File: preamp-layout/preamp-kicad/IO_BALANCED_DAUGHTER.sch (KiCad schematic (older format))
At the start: 49 parts, among them J29 XLR3, J30 XLR3, J31 Conn_01x03_Male, J32 Conn_01x03_Female, J33 Conn_01x03_Female, J34 Conn_01x03_Male, J35 XLR3, J36 XLR3, U6 TL072, U7 TL072, U8 TL072

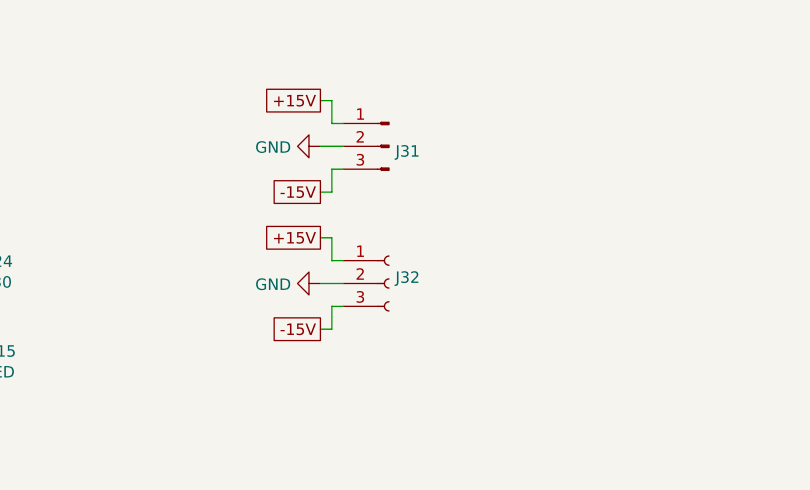
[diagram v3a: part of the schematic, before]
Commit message: power headers updated, slight BOM update
changed footprint on all 5V, +-15V to JST B2B / B3B connectors. All male conns now.
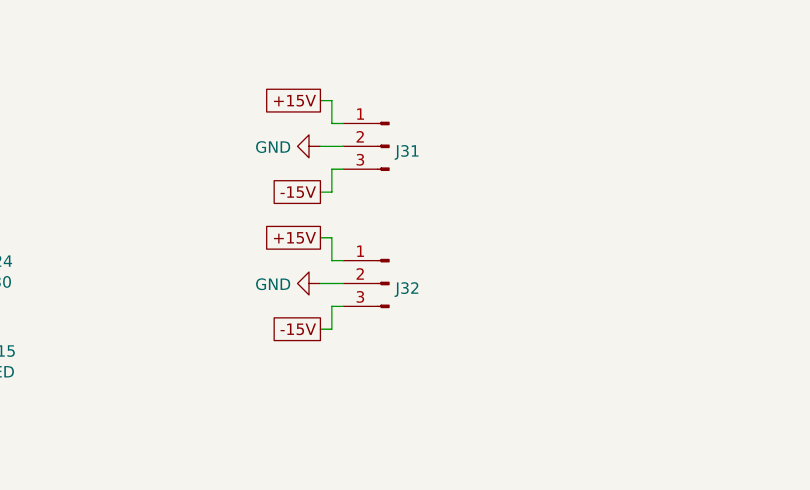
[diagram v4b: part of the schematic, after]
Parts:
- removed J32: Conn_01x03_Female, Connector_PinHeader_2.54mm:PinHeader_1x03_P2.54mm_Vertical, symbol Connector:Conn_01x03_Female
- added J32: Conn_01x03_Male, Connector_JST:JST_EH_B3B-EH-A_1x03_P2.50mm_Vertical, symbol Connector:Conn_01x03_Male
- J31: footprint Connector_PinHeader_2.54mm:PinHeader_1x03_P2.54mm_Vertical -> Connector_JST:JST_EH_B3B-EH-A_1x03_P2.50mm_Vertical
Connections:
- net +15V: now also J32.1 (Pin_1)
- net -15V: now also J32.3 (Pin_3)
- net GND: now also J32.2 (Pin_2)
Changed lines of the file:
@@
 F 0 "J31" H 5872 6078 50  0000 R CNN
 F 1 "Conn_01x03_Male" H 5872 6033 50  0001 R CNN
-F 2 "Connector_PinHeader_2.54mm:PinHeader_1x03_P2.54mm_Vertical" H 5900 6100 50  0001 C CNN
+F 2 "Connector_JST:JST_EH_B3B-EH-A_1x03_P2.50mm_Vertical" H 5900 6100 50  0001 C CNN
 F 3 "~" H 5900 6100 50  0001 C CNN
 	1    5900 6100
 	-1   0    0    -1
-$EndComp
-$Comp
-L Connector:Conn_01x03_Female J?
-U 1 1 64789768
-P 5900 6700
-AR Path="/5E607732/64789768" Ref="J?"  Part="1"
-AR Path="/5E2D8DA2/64789768" Ref="J?"  Part="1"
-AR Path="/6009D432/64789768" Ref="J?"  Part="1"
-AR Path="/5E1A0CE1/64789768" Ref="J32"  Part="1"
-F 0 "J32" H 5928 6726 50  0000 L CNN
-F 1 "Conn_01x03_Female" H 5928 6635 50  0001 L CNN
-F 2 "Connector_PinHeader_2.54mm:PinHeader_1x03_P2.54mm_Vertical" H 5900 6700 50  0001 C CNN
-F 3 "~" H 5900 6700 50  0001 C CNN
-	1    5900 6700
-	1    0    0    -1
 $EndComp
 Wire Wire Line
@@
 	1    0    0    -1
 $EndComp
+$Comp
+L Connector:Conn_01x03_Male J?
+U 1 1 5E5911E4
+P 5900 6700
+AR Path="/5E27B612/5E5911E4" Ref="J?"  Part="1"
+AR Path="/6009D432/5E5911E4" Ref="J?"  Part="1"
+AR Path="/5E1A0CE1/5E5911E4" Ref="J32"  Part="1"
+F 0 "J32" H 5872 6678 50  0000 R CNN
+F 1 "Conn_01x03_Male" H 5872 6633 50  0001 R CNN
+F 2 "Connector_JST:JST_EH_B3B-EH-A_1x03_P2.50mm_Vertical" H 5900 6700 50  0001 C CNN
+F 3 "~" H 5900 6700 50  0001 C CNN
+	1    5900 6700
+	-1   0    0    -1
+$EndComp
 $EndSCHEMATC

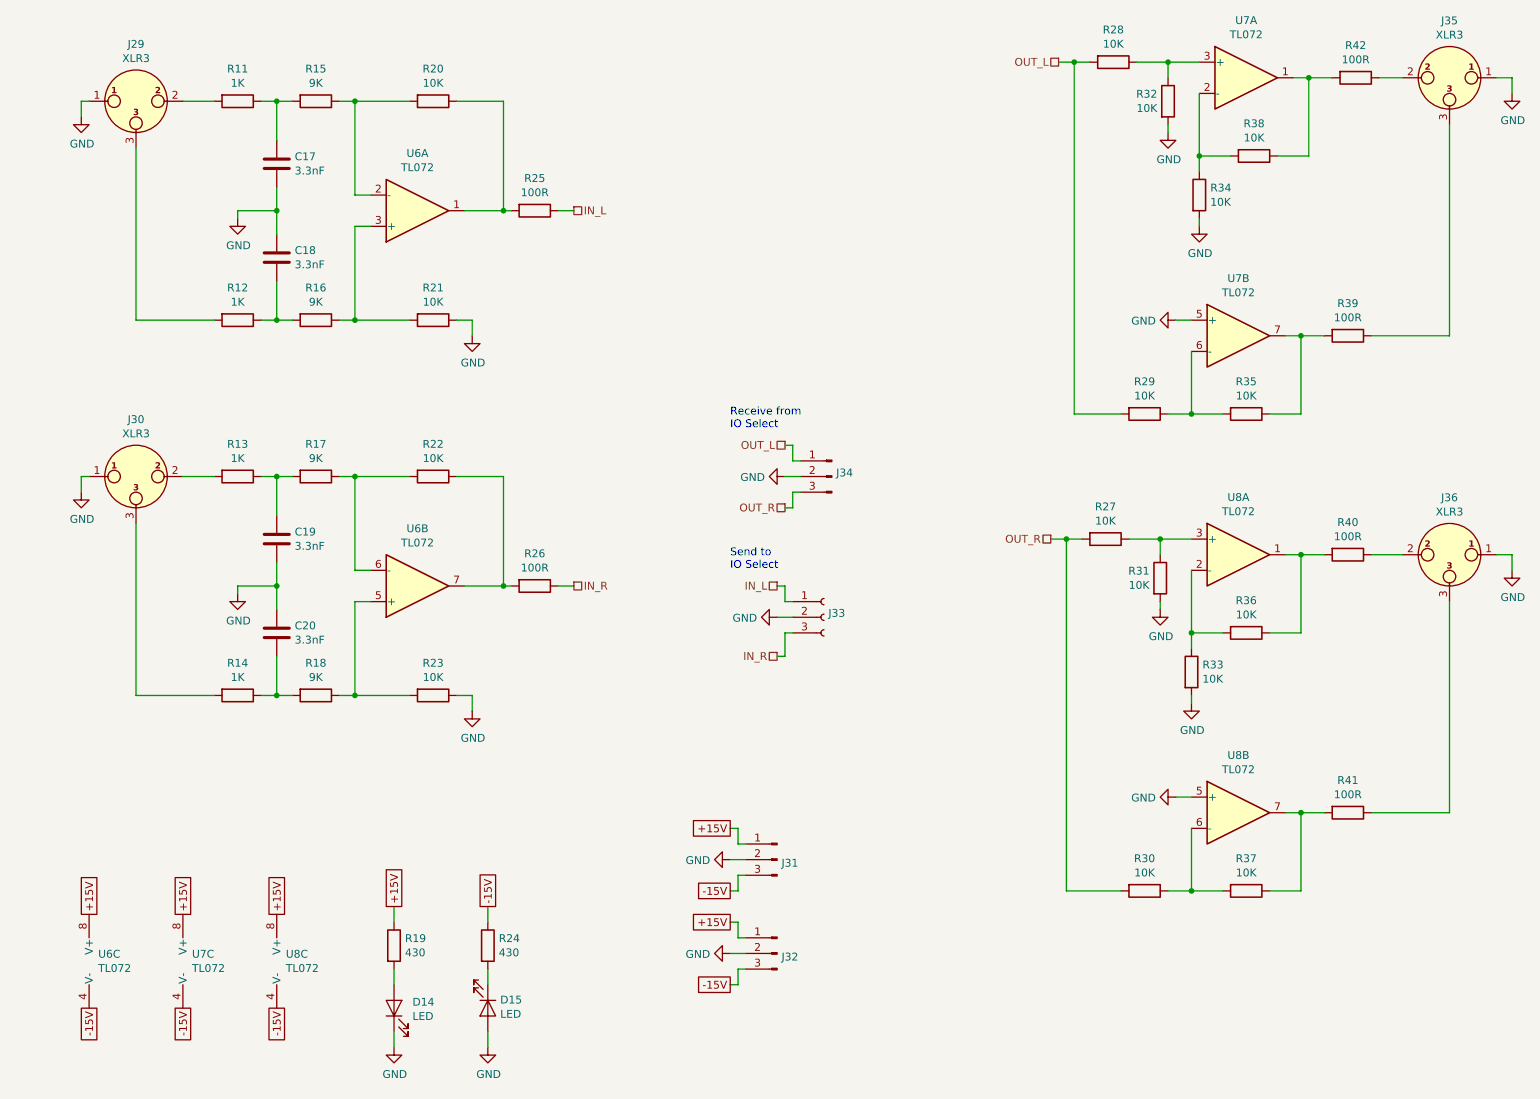
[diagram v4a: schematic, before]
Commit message: Transformer specification
updated schematic, BOM with power transformer info. Other minor schematic tweaks.
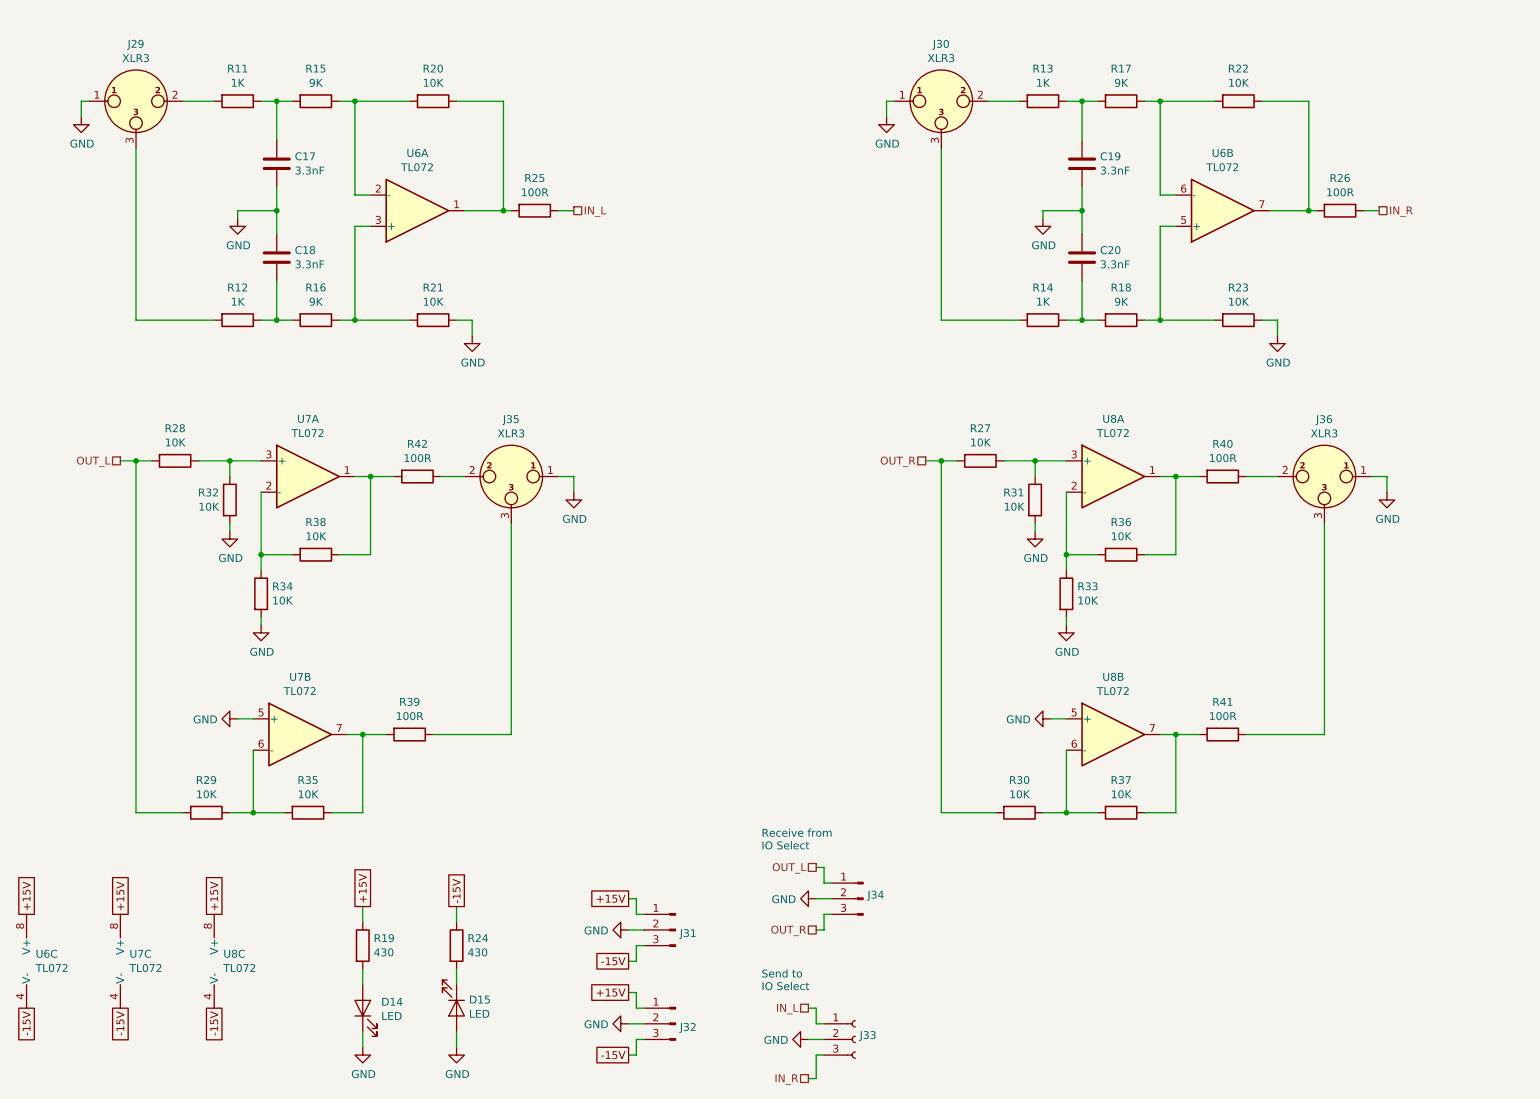
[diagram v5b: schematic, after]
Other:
- moved on the sheet: C19, C20, D14, D15, J30, J31, J32, J33, J34, J35, J36, R13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

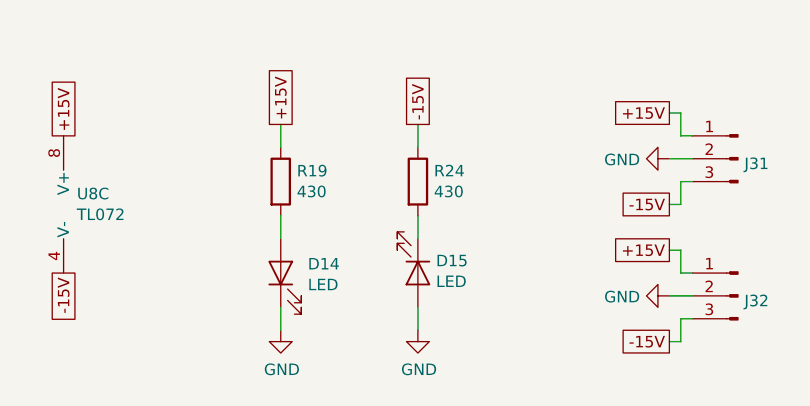
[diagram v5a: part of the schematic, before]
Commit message: Added front panel LED sheet. BOM update. Front panel PCA work
other minor changes like LED color assignments, etc
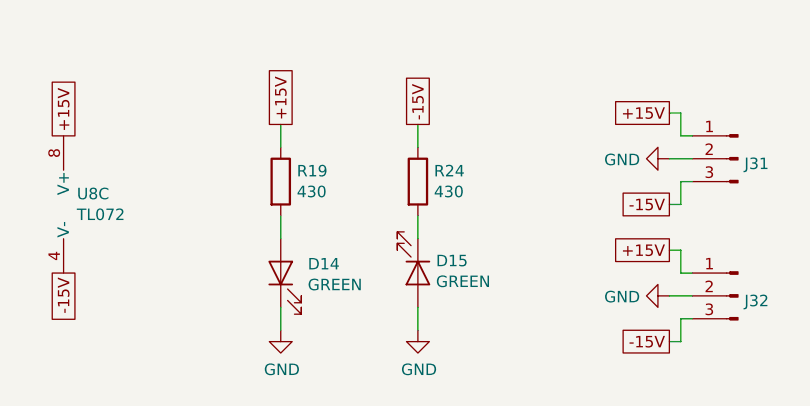
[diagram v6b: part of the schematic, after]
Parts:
- D14, D15: value LED -> GREEN
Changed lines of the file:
@@
 $Descr A4 11693 8268
 encoding utf-8
-Sheet 8 11
+Sheet 8 12
 Title "Balanced IO Daughter Board"
 Date "2020-01-23"
@@
 AR Path="/5E80BFEC/5E50A285" Ref="D?"  Part="1"
 F 0 "D14" V 3289 6932 50  0000 R CNN
-F 1 "LED" V 3198 6932 50  0000 R CNN
+F 1 "GREEN" V 3198 6932 50  0000 R CNN
 F 2 "LED_SMD:LED_1206_3216Metric_Pad1.42x1.75mm_HandSolder" H 3250 7050 50  0001 C CNN
 F 3 "~" H 3250 7050 50  0001 C CNN
@@
 AR Path="/5E80BFEC/5E50A295" Ref="D?"  Part="1"
 F 0 "D15" V 3797 7129 50  0000 L CNN
-F 1 "LED" V 3888 7129 50  0000 L CNN
+F 1 "GREEN" V 3888 7129 50  0000 L CNN
 F 2 "LED_SMD:LED_1206_3216Metric_Pad1.42x1.75mm_HandSolder" H 3850 7050 50  0001 C CNN
 F 3 "~" H 3850 7050 50  0001 C CNN
